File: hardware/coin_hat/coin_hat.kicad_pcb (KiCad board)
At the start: 2 copper layers, 65 x 90 mm, 0 parts

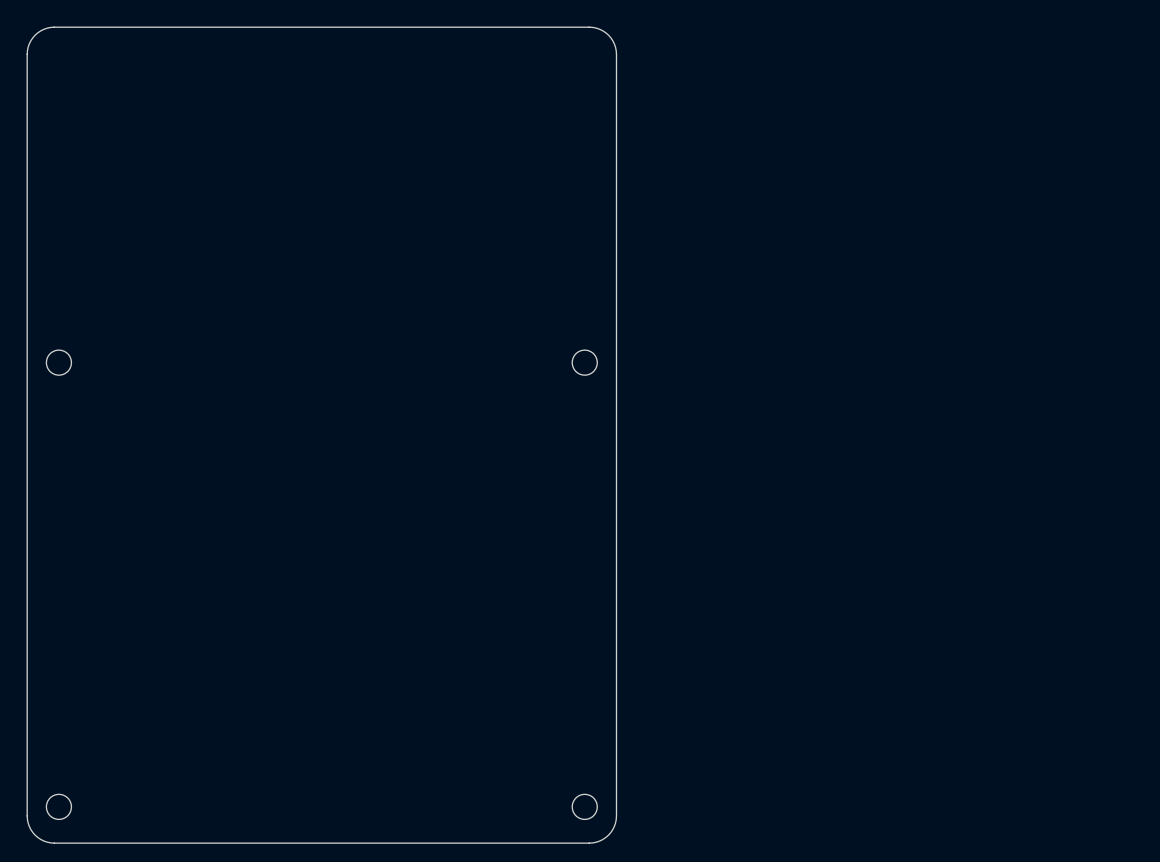
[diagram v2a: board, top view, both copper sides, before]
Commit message: coin_hat rev 1: servo diverter on its own buck, board runs lengthwise
The diverter is now the MG996R servo, not a stepper: drop the third
StepStick socket, its jumpers, motor connector and home switch, and add
a separate 12V->5-6V buck (U8) for a +SERVO rail, a 3-pin servo header
on GP6 (driven directly), 1000uF at the connector, a rail-live LED and
a GP27 rail sense. A dead servo rail with GP6 pulsing back-powers the
servo through its signal pin and looks like a signal fault.

The outline now runs along the Pi: 109 x 56.5, with a 44 mm overhang
past the SD end instead of 33.5 mm off the header edge. It also fixes
two rev 0 errors against the HAT+ spec: the header was 1.27 mm off in
both axes, and there was no notch for the Pi 5 camera/display FPCs.

Co-Authored-By: Claude Opus 5.5 <noreply@anthropic.com>
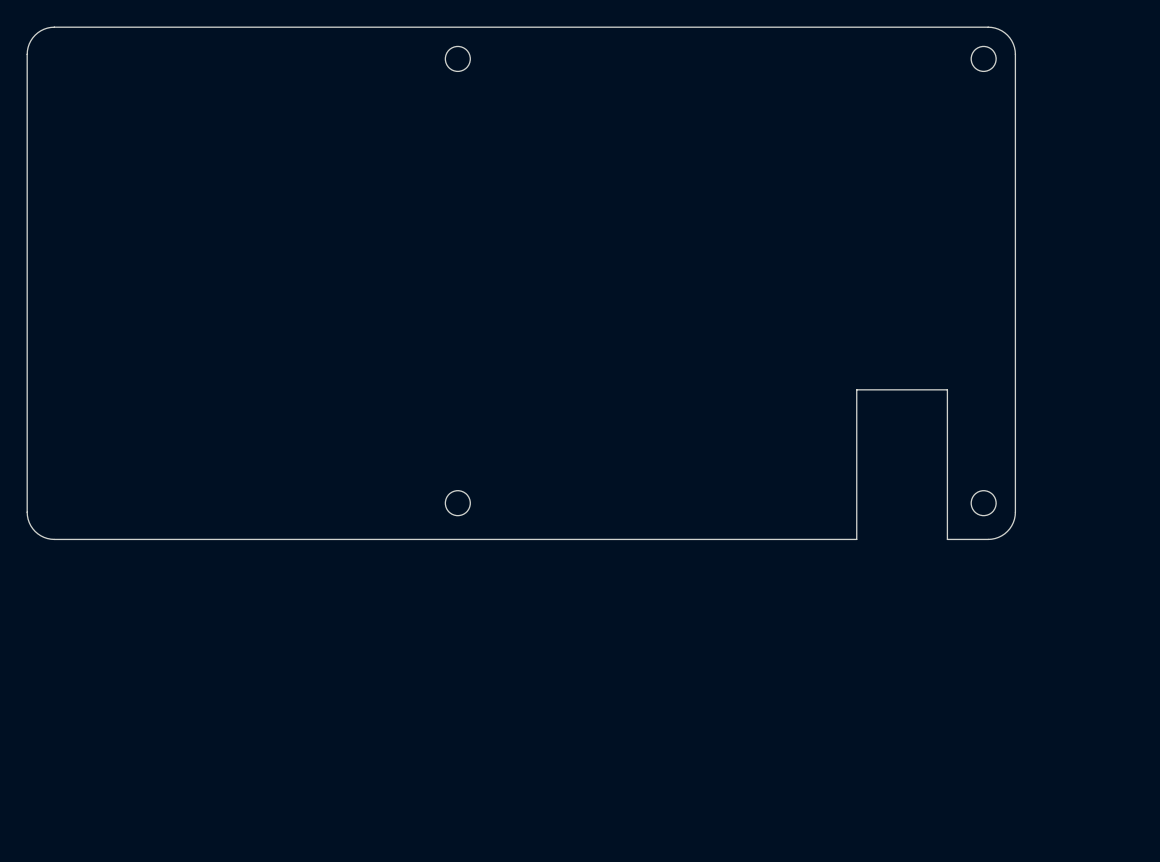
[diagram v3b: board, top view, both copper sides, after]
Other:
- board size 65 x 90 mm -> 109 x 56.5 mm
- board text added: "(Pi + Pico)"
- board text added: "10 x 16.5"
- board text added: "1000u AT J4"
- board text added: "16 mm board-to-board spacers (HAT+ spec, Active Cooler). Pi + HAT stack is 129 x 56.5 overall."
- board text added: "C2 D1"
- board text added: "CSI/DSI"
- board text added: "Coin sorter HAT+ rev 1 - 109 x 56.5, runs lengthwise: HAT+ holes/header at the right, 44 mm overhang past the SD end"
- board text added: "D5 R15-R17"
- board text added: "F1 D2 C1"
- board text added: "FPC notch"
- board text added: "J1 2x20 socket, BOTTOM side. pin1 (3V3) at Pi (8.37, 4.77), pin2 (5V) at (8.37, 2.23) - HAT+ spec: header centre 29 mm from hole"
- board text added: "J2 J3 motor XH"
- board text added: "J4 servo + C6"
- board text added: "J5 12V jack (plug"
- board text added: "J6 J7 J9 J10 J11 J12 along the bottom edge"
- board text added: "PCIe FFC is"
- board text added: "Pi 5 PoE hdr (keep bottom clear)"
- board text added: "Pi 5 short edge (SD card / PCIe FFC end). Left of this line nothing is under the board."
- board text added: "Q1-Q3, U6, U7, JP1"
- board text added: "StepSticks + C3 C4"
- board text added: "U1 Pico (51x21) over the Pi. Top-side parts only here: bottom faces the SoC / active cooler"
- board text added: "U2 belt, U3 feeder"
- board text added: "U5 5V buck"
- board text added: "U8 servo buck"
- board text added: "at the left end"
- board text added: "beneath here"
- board text added: "from left end)"
- board text removed: "Coin sorter HAT+ rev 0 - 65 x 90, HAT+ hole pattern at the Pi end, 33.5 mm overhang for drivers and power"
- board text removed: "J1 2x20 socket, BOTTOM side. pin1 (3V3) at (7.1, 39.54), pin2 (5V) at (7.1, 37.00) - verify vs HAT+ spec"
- board text removed: "J5 jack + F1"
- board text removed: "Pi 5 edge (header side). Above this line nothing is under the board."
- board text removed: "Q1-Q3, U6, U7 + connectors J6-J12 along the bottom/side edges"
- board text removed: "U1 Pico (51x21), over the Pi. Keep under 5 mm tall here: Pi 5 SoC/cooler is beneath"
- board text removed: "U2 U3 U4 StepSticks + C3-C5, motor XH J2-J4 along the top edge"
- board text removed: "U5 buck, C1 C2, D1 D2"

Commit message: coin_hat: fix diode polarity and StepStick pinout, size board to fit
Checked with KiCad 9 (ERC, DRC, symbol pin vs footprint pad). Three
pin-numbering bugs carried over from rev 0 would have shipped broken:

- Diode symbols had the anode on pin 1; KiCad footprints put the
  cathode there. D3/D4 flybacks would short 12V to ground when the key
  light or aux output switched on, D1 would block the Pico's VSYS and
  the servo-rail LED would never light.
- The StepStick symbol numbered pins 1=EN..16=GND, but the
  Pololu_Breakout-16 footprint is 1=GND..16=DIR, so every driver pin,
  VMOT included, landed on the wrong pad.
- Neither Pololu buck matches the generic 1x5 footprint used for U5/U8
  (D24V50F5 has no PG, D36V28Fx has 6 pads). Flagged for redraw.

Packing the real courtyards (bucks are 17.8 x 20.3) showed the 44 mm
overhang cannot fit; 57 mm is the shortest clean floor plan. Board is
now 122 x 56.5 with that floor plan on User.Comments.

Co-Authored-By: Claude Opus 5.5 <noreply@anthropic.com>
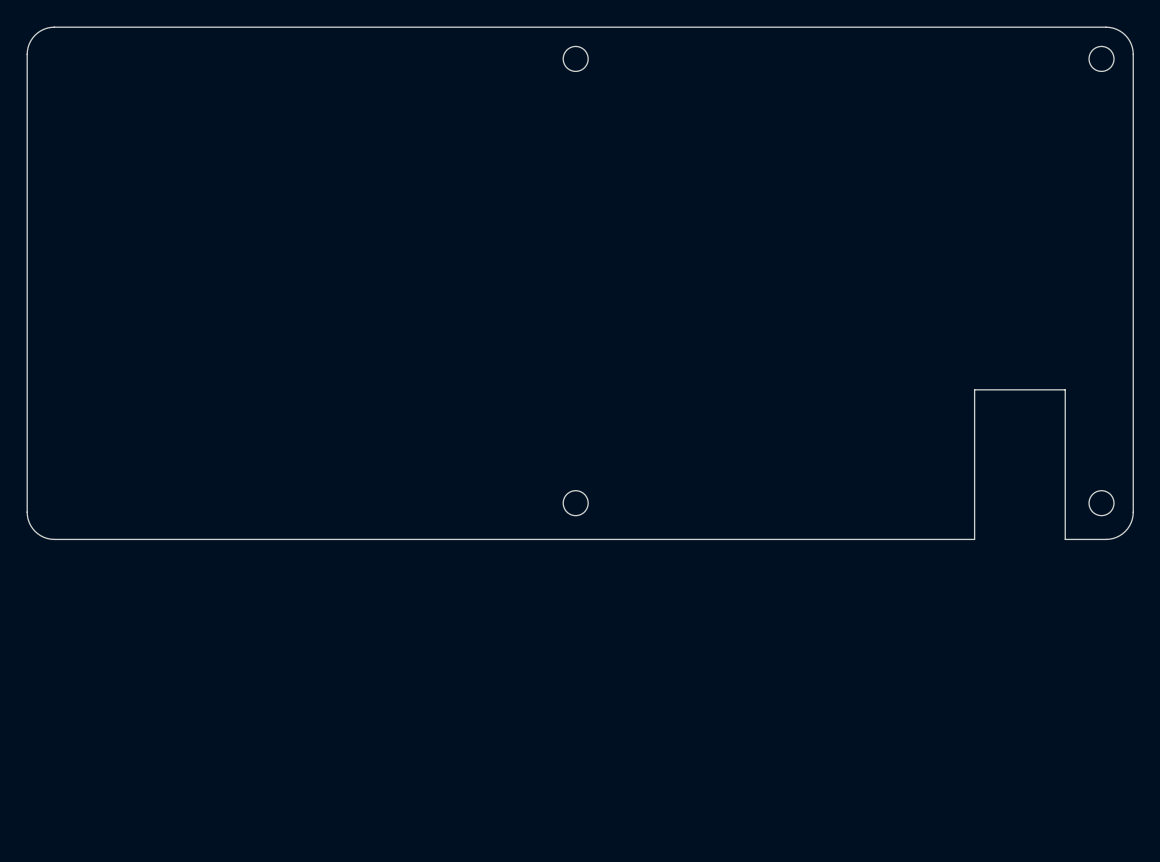
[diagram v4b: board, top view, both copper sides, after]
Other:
- board size 109 x 56.5 mm -> 122 x 56.5 mm
- board text added: "C1"
- board text added: "C2"
- board text added: "C3"
- board text added: "C4"
- board text added: "C6"
- board text added: "CSI/DSI FPC"
- board text added: "Coin sorter HAT+ rev 1 - 122 x 56.5, runs lengthwise: HAT+ holes/header at the right, 57 mm overhang past the SD end"
- board text added: "D1"
- board text added: "D2"
- board text added: "D5 R15-17"
- board text added: "F1"
- board text added: "Floor plan = real courtyards (bucks = module outline), checked for overlaps. 16 mm spacers. Pi + HAT stack 142 x 56.5."
- board text added: "J1 2x20 socket, BOTTOM side. pin1 (3V3) at Pi (8.37, 4.77), pin2 (5V) at (8.37, 2.23). PCIe FFC under the Pi edge, below the left hole"
- board text added: "J10"
- board text added: "J11"
- board text added: "J12"
- board text added: "J2"
- board text added: "J3"
- board text added: "J4"
- board text added: "J5 jack (plug from left)"
- board text added: "J6"
- board text added: "J7"
- board text added: "J9"
- board text added: "JP21-24"
- board text added: "JP31-34"
- board text added: "Pi 5 PoE"
- board text added: "Q1 Q2 D3 D4"
- board text added: "Q3 U6 U7 JP1 R1-R14"
- board text added: "U1 Pico"
- board text added: "U2"
- board text added: "U3"
- board text added: "U5 5V buck 17.8x20.3"
- board text added: "U8 servo buck 17.8x20.3"
- board text added: "notch 10x16.5"
- board text removed: "(Pi + Pico)"
- board text removed: "10 x 16.5"
- board text removed: "1000u AT J4"
- board text removed: "16 mm board-to-board spacers (HAT+ spec, Active Cooler). Pi + HAT stack is 129 x 56.5 overall."
- board text removed: "C2 D1"
- board text removed: "CSI/DSI"
- board text removed: "Coin sorter HAT+ rev 1 - 109 x 56.5, runs lengthwise: HAT+ holes/header at the right, 44 mm overhang past the SD end"
- board text removed: "D5 R15-R17"
- board text removed: "F1 D2 C1"
- board text removed: "FPC notch"
- board text removed: "J1 2x20 socket, BOTTOM side. pin1 (3V3) at Pi (8.37, 4.77), pin2 (5V) at (8.37, 2.23) - HAT+ spec: header centre 29 mm from hole"
- board text removed: "J2 J3 motor XH"
- board text removed: "J4 servo + C6"
- board text removed: "J5 12V jack (plug"
- board text removed: "J6 J7 J9 J10 J11 J12 along the bottom edge"
- board text removed: "PCIe FFC is"
- board text removed: "Pi 5 PoE hdr (keep bottom clear)"
- board text removed: "Q1-Q3, U6, U7, JP1"
- board text removed: "StepSticks + C3 C4"
- board text removed: "U1 Pico (51x21) over the Pi. Top-side parts only here: bottom faces the SoC / active cooler"
- board text removed: "U2 belt, U3 feeder"
- board text removed: "U5 5V buck"
- board text removed: "U8 servo buck"
- board text removed: "at the left end"
- board text removed: "beneath here"
- board text removed: "from left end)"

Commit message: coin_hat: draw Pololu buck footprints from the drill guides
U5 and U8 were a generic 1x5 header that matched neither module. Add a
project footprint library (coin_hat.pretty + fp-lib-table) with
Pololu_D24V50F5 and Pololu_D36V28Fx, placing pads and #2 mounting holes
at the coordinates in Pololu's drill-guide DXFs (reg15d01, reg24g), top
view, pad 1 = EN:

  D24V50F5  EN VIN GND GND VOUT
  D36V28Fx  EN VIN GND GND VOUT, PG 0.1" inboard of EN

Replace the generic Buck symbol with one symbol per module. EN is left
open (100k pull-up to VIN on both modules) and PG is unused. ERC is
clean, every pin maps to a pad, and the floor plan still packs with the
real 18.4 x 20.9 courtyards.

Co-Authored-By: Claude Opus 5.5 <noreply@anthropic.com>
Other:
- board text added: "Floor plan = real courtyards (incl. coin_hat:Pololu_* footprints), checked for overlaps. 16 mm spacers. Pi + HAT stack 142 x 56.5."
- board text added: "U5 5V buck D24V50F5"
- board text added: "U8 servo buck D36V28Fx"
- board text removed: "Floor plan = real courtyards (bucks = module outline), checked for overlaps. 16 mm spacers. Pi + HAT stack 142 x 56.5."
- board text removed: "U5 5V buck 17.8x20.3"
- board text removed: "U8 servo buck 17.8x20.3"
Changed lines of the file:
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@@
   (gr_rect (start 96.2 101) (end 103.6 105.6) (stroke (width 0.15) (type dash)) (fill none) (layer "Cmts.User"))
   (gr_text "D2" (at 96.7 102.5 0) (layer "Cmts.User") (effects (font (size 0.8 0.8) (thickness 0.12)) (justify left)))
-  (gr_rect (start 87.5 50.5) (end 105.3 70.8) (stroke (width 0.15) (type dash)) (fill none) (layer "Cmts.User"))
-  (gr_text "U5 5V buck 17.8x20.3" (at 88 52 0) (layer "Cmts.User") (effects (font (size 0.8 0.8) (thickness 0.12)) (justify left)))
-  (gr_rect (start 87.5 71.2) (end 96.1 79.8) (stroke (width 0.15) (type dash)) (fill none) (layer "Cmts.User"))
-  (gr_text "C2" (at 88 72.7 0) (layer "Cmts.User") (effects (font (size 0.8 0.8) (thickness 0.12)) (justify left)))
+  (gr_rect (start 87.5 50.5) (end 105.9 71.4) (stroke (width 0.15) (type dash)) (fill none) (layer "Cmts.User"))
+  (gr_text "U5 5V buck D24V50F5" (at 88 52 0) (layer "Cmts.User") (effects (font (size 0.8 0.8) (thickness 0.12)) (justify left)))
+  (gr_rect (start 87.5 71.8) (end 96.1 80.4) (stroke (width 0.15) (type dash)) (fill none) (layer "Cmts.User"))
+  (gr_text "C2" (at 88 73.3 0) (layer "Cmts.User") (effects (font (size 0.8 0.8) (thickness 0.12)) (justify left)))
   (gr_rect (start 96.5 72) (end 103.6 75.6) (stroke (width 0.15) (type dash)) (fill none) (layer "Cmts.User"))
   (gr_text "D1" (at 97 73.5 0) (layer "Cmts.User") (effects (font (size 0.8 0.8) (thickness 0.12)) (justify left)))
-  (gr_rect (start 78 84.5) (end 95.8 104.8) (stroke (width 0.15) (type dash)) (fill none) (layer "Cmts.User"))
-  (gr_text "U8 servo buck 17.8x20.3" (at 78.5 86 0) (layer "Cmts.User") (effects (font (size 0.8 0.8) (thickness 0.12)) (justify left)))
+  (gr_rect (start 77.7 84.5) (end 96.1 105.4) (stroke (width 0.15) (type dash)) (fill none) (layer "Cmts.User"))
+  (gr_text "U8 servo buck D36V28Fx" (at 78.2 86 0) (layer "Cmts.User") (effects (font (size 0.8 0.8) (thickness 0.12)) (justify left)))
   (gr_rect (start 96.2 80.5) (end 106.8 91.1) (stroke (width 0.15) (type dash)) (fill none) (layer "Cmts.User"))
   (gr_text "C6" (at 96.7 82 0) (layer "Cmts.User") (effects (font (size 0.8 0.8) (thickness 0.12)) (justify left)))
@@
   (gr_text "Pi 5 PoE" (at 165 93.5 0) (layer "Cmts.User") (effects (font (size 0.6 0.6) (thickness 0.12)) (justify left)))
   (gr_text "Coin sorter HAT+ rev 1 - 122 x 56.5, runs lengthwise: HAT+ holes/header at the right, 57 mm overhang past the SD end" (at 50 110.5 0) (layer "Cmts.User") (effects (font (size 1.2 1.2) (thickness 0.15)) (justify left)))
-  (gr_text "Floor plan = real courtyards (bucks = module outline), checked for overlaps. 16 mm spacers. Pi + HAT stack 142 x 56.5." (at 50 113 0) (layer "Cmts.User") (effects (font (size 1.0 1.0) (thickness 0.12)) (justify left)))
+  (gr_text "Floor plan = real courtyards (incl. coin_hat:Pololu_* footprints), checked for overlaps. 16 mm spacers. Pi + HAT stack 142 x 56.5." (at 50 113 0) (layer "Cmts.User") (effects (font (size 1.0 1.0) (thickness 0.12)) (justify left)))
 )
